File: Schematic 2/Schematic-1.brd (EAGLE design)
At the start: 127.2 x 80.2 mm, 37 parts, among them IC1 7805T, IC3 MCP23017SO, Q1 BSS138, Q2 BSS138, U2 LMV358, U3 LMV324

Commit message: Final tweaks to plugable Tiva board
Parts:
- moved R4 1.38 mm to (55.8, 4.18)
- moved R1 1.32 mm to (55.5, 9.76)
- moved R3 0.20 mm to (55.6, 15.1)
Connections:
- new net N$9: IC3.22, JP4.2
- net N$3: no longer IC3.22
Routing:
- net 37: track 63.5 -> 107.0 mm, vias 5 -> 0
- net 27: track 65.9 -> 100.7 mm, vias 4 -> 2
- net N2: track 97.4 -> 127.4 mm, vias 4 -> 2
- net SCL: track 143.5 -> 113.9 mm, vias 6 -> 8
- net N$9: track 0.00 -> 29.1 mm, vias 0 -> 1
- net 38: track 102.8 -> 75.6 mm, vias 3 -> 2
- net SDA: track 153.8 -> 179.7 mm, vias 6 -> 2
- net 5V1: track 182.7 -> 207.3 mm, vias 6 -> 4
- net 15: track 159.7 -> 135.4 mm
- net 31: track 39.2 -> 62.9 mm
- net 39: track 82.9 -> 65.4 mm, vias 4 -> 3
- net 28: track 39.2 -> 56.4 mm, vias 0 -> 2
- net PB4: track 90.6 -> 74.9 mm
- net PB7: track 92.6 -> 77.2 mm, vias 1 -> 0
- net 30: track 52.1 -> 36.8 mm, vias 4 -> 1
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- added copper zone on layer 1, net GND
- added copper zone on layer 16, net GND
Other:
- board size 127.2 x 80.2 mm -> 127.2 x 82.1 mm
- board text added: "1"
- board text added: "16"
- board text added: "17A"
- board text added: "17B"
- board text added: "3.3V"
- board text added: "55"
- board text added: "57"
- board text added: "5V"
- board text added: "74"
- board text added: "GND"
- board text added: "PORT A"
- board text added: "PORT B"
- board text added: "VBUS"

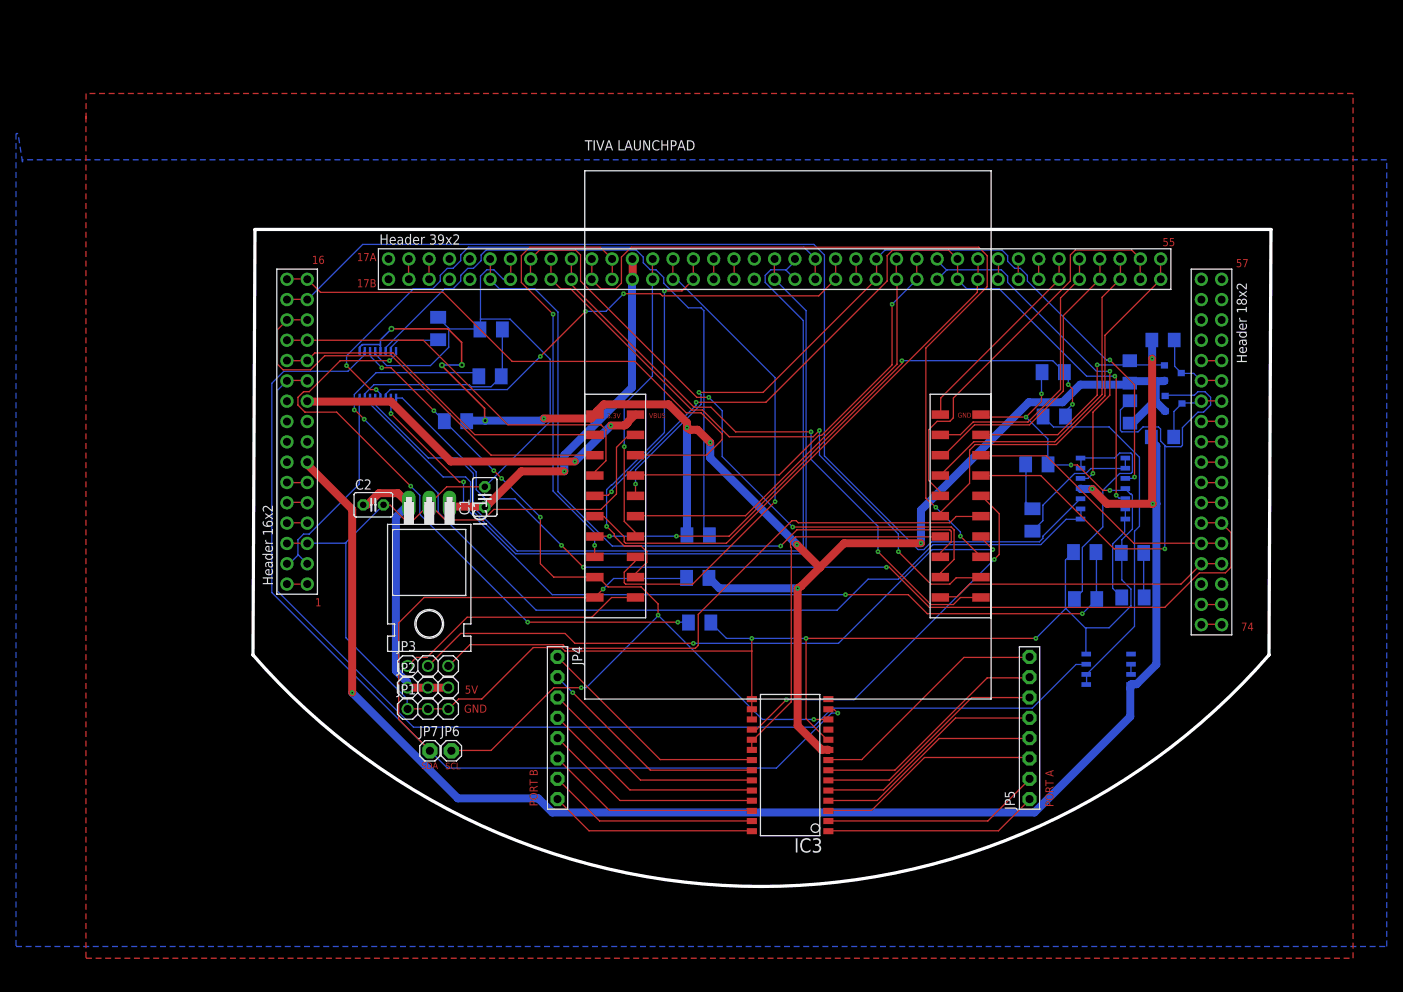
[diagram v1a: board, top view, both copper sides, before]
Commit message: Plugable TIVA board at 17:46
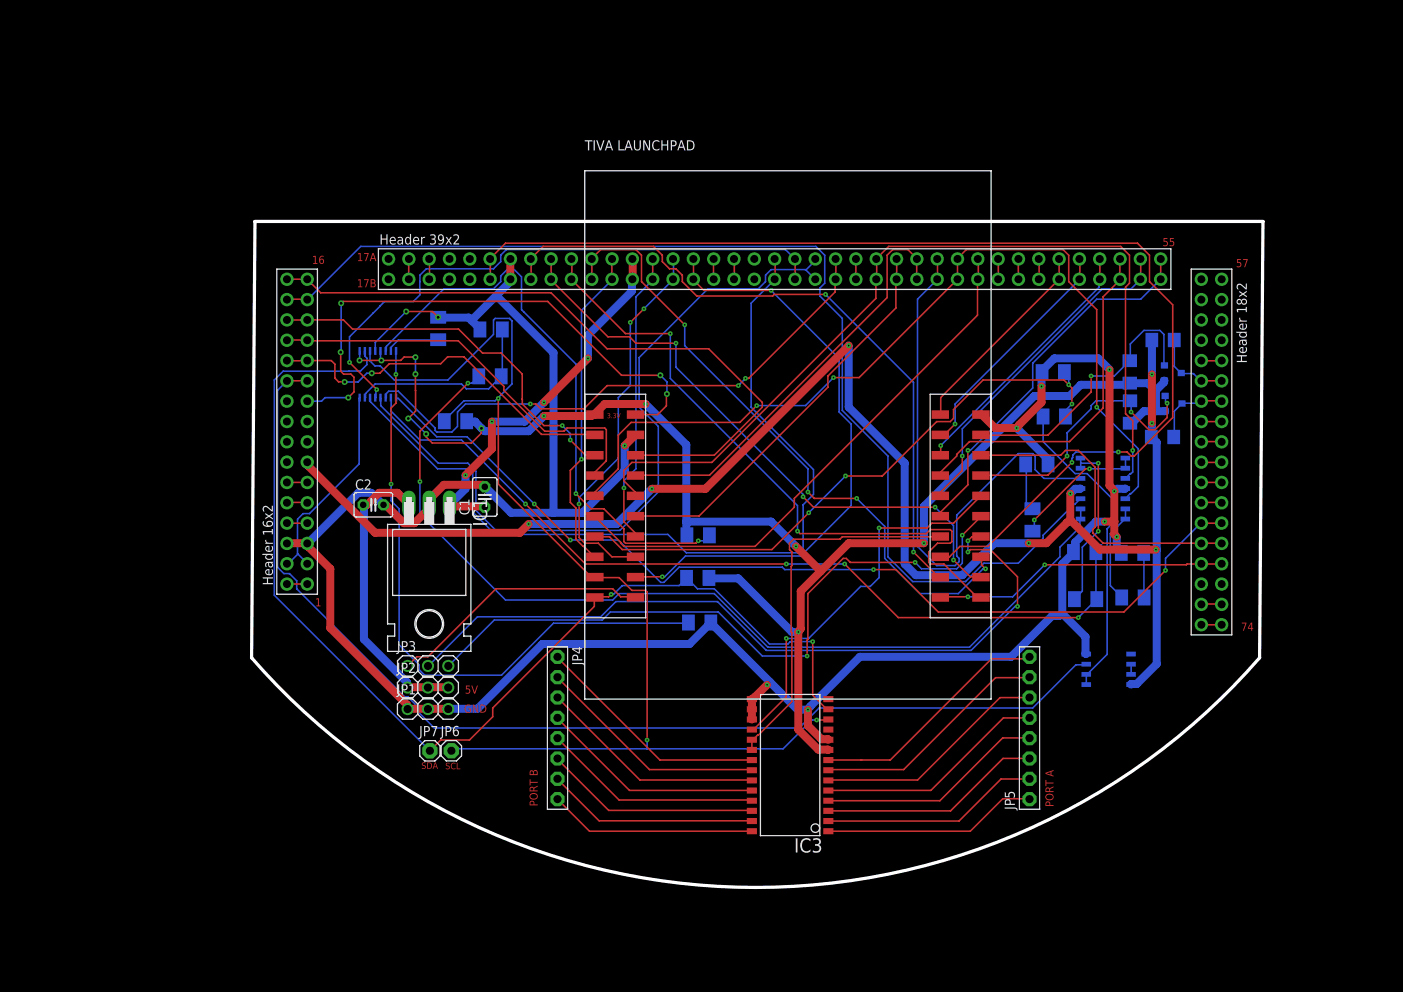
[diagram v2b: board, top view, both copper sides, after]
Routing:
- net 22: track 91.9 -> 145.1 mm, vias 1 -> 2
- net SDA: track 179.7 -> 140.2 mm
- net PF0: track 68.1 -> 34.8 mm, vias 1 -> 3
- net 37: track 107.0 -> 74.3 mm, vias 0 -> 2
- net SCL: track 113.9 -> 146.1 mm, vias 8 -> 3
- net 44: track 45.2 -> 70.3 mm, vias 2 -> 0
- net 32: track 49.5 -> 74.6 mm
- net 5V2: track 46.6 -> 71.1 mm, vias 2 -> 5
- net 27: track 100.7 -> 80.6 mm, vias 2 -> 4
- net 38: track 75.6 -> 94.2 mm, vias 2 -> 0
- net PB6: track 79.9 -> 96.5 mm, vias 2 -> 3
- net 28: track 56.4 -> 40.8 mm, vias 2 -> 1
- net 31: track 62.9 -> 47.8 mm, vias 1 -> 3
- net GND: track 335.9 -> 323.2 mm, vias 7 -> 11
- net 41: track 100.3 -> 110.9 mm, vias 4 -> 1
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- removed copper zone on layer 1, net GND
- removed copper zone on layer 16, net GND
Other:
- board size 127.2 x 82.1 mm -> 126.4 x 83.3 mm
- board text removed: "VBUS"

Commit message: Plugable TIVA changes on 10-6-2017
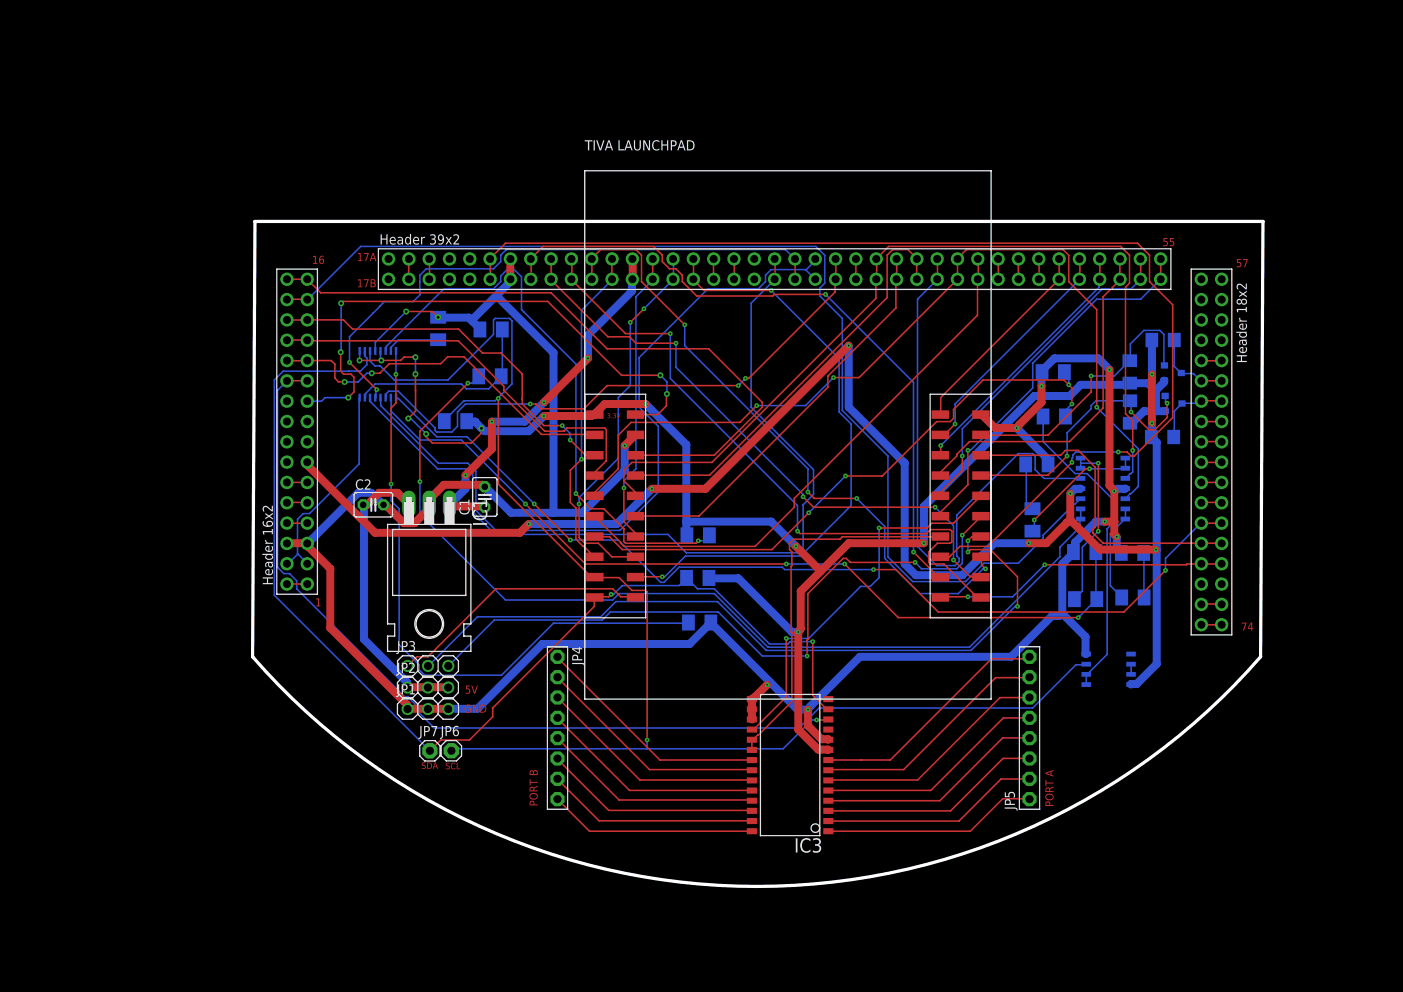
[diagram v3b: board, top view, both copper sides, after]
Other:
- board size 126.4 x 83.3 mm -> 126.3 x 83.1 mm
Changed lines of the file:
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@@
 <board>
 <plain>
-<wire x1="0.182" y1="54.32" x2="-0.2398" y2="-0.2189" width="0.4064" layer="20"/>
-<wire x1="125.7602" y1="-0.2189" x2="126.182" y2="54.32" width="0.4064" layer="20"/>
+<wire x1="0.182" y1="54.32" x2="-0.1134" y2="-0.0924" width="0.4064" layer="20"/>
+<wire x1="125.8866" y1="-0.0924" x2="126.182" y2="54.32" width="0.4064" layer="20"/>
 <wire x1="126.182" y1="54.32" x2="0.182" y2="54.32" width="0.4064" layer="20"/>
-<wire x1="125.7602" y1="-0.2189" x2="-0.2398" y2="-0.2189" width="0.4064" layer="20" curve="-98.003115"/>
+<wire x1="125.8866" y1="-0.0924" x2="-0.1134" y2="-0.0924" width="0.4064" layer="20" curve="-98.003115"/>
 <text x="20.97" y="-14.111" size="0.8128" layer="1">SDA</text>
 <text x="23.966" y="-14.158" size="0.8128" layer="1">SCL</text>

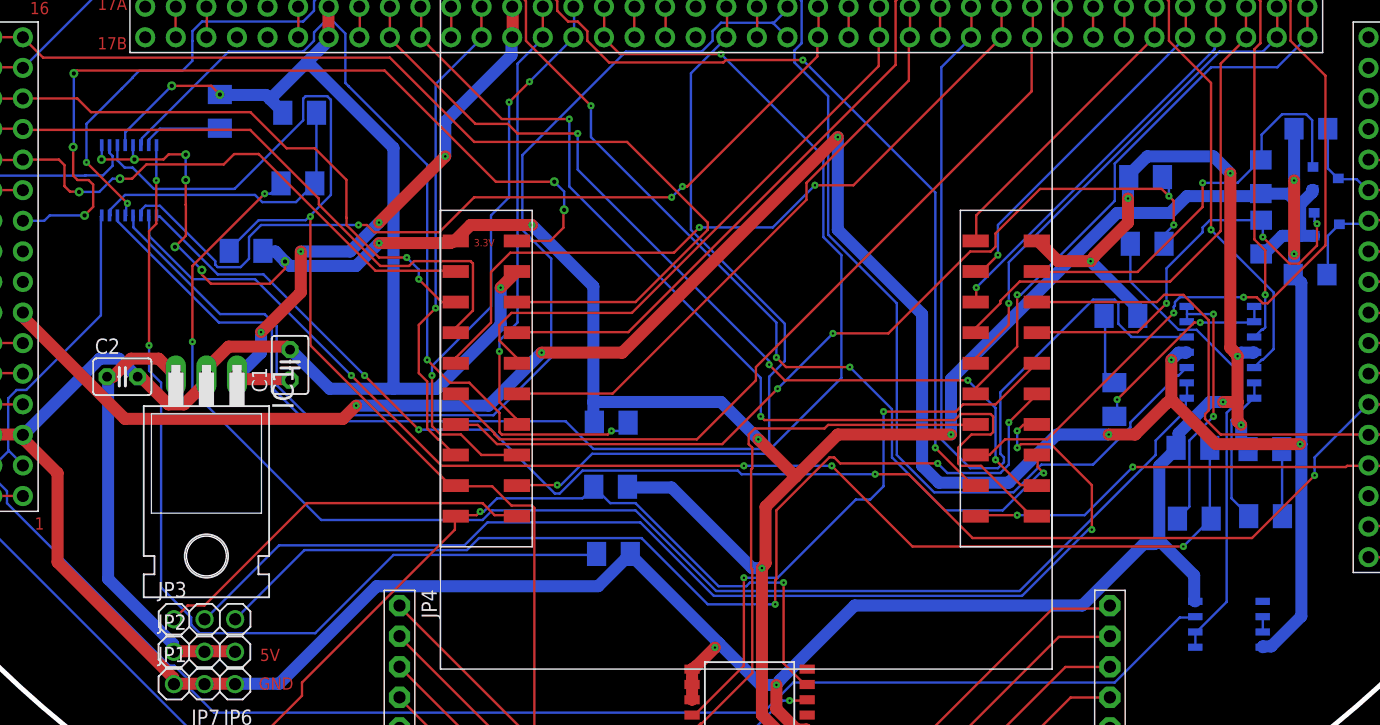
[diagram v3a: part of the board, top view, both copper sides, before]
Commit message: Plugable Tiva board changes at 14:26 on 10-06-2017
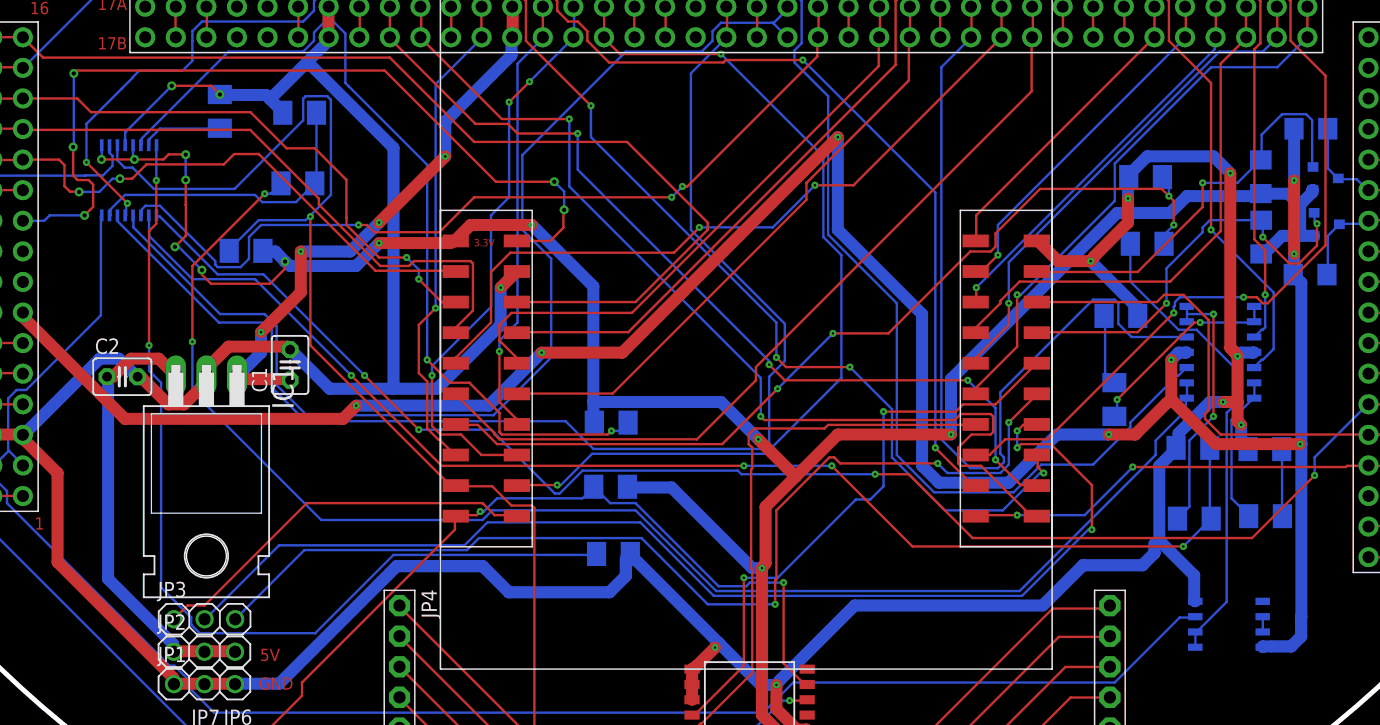
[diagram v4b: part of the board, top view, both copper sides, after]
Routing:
- net GND: track 323.2 -> 326.3 mm
- net 5V1: track 197.8 -> 198.8 mm
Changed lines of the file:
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@@
 <wire x1="107.3" y1="21" x2="107.6" y2="20.6" width="1" layer="1"/>
 <wire x1="75.8" y1="-0.1" x2="69.6" y2="-6.3" width="1" layer="16"/>
-<wire x1="94.7" y1="-0.1" x2="75.8" y2="-0.1" width="1" layer="16"/>
-<wire x1="99.8" y1="5" x2="94.7" y2="-0.1" width="1" layer="16"/>
-<wire x1="100.7" y1="5" x2="99.8" y2="5" width="1" layer="16"/>
+<wire x1="91.4235" y1="-0.1" x2="75.8" y2="-0.1" width="1" layer="16"/>
 <wire x1="69.6" y1="-6.3" x2="69.3" y2="-6.7" width="1" layer="16"/>
 <wire x1="100.7" y1="5" x2="101.1" y2="5.3" width="1" layer="16"/>
@@
 <wire x1="22.1" y1="19.5" x2="21.964" y2="18.996" width="1" layer="1"/>
 <wire x1="28.9" y1="21.2" x2="28.909" y2="21.15" width="1" layer="1"/>
-<wire x1="54.5" y1="1.5" x2="56.8" y2="3.8" width="1" layer="16"/>
-<wire x1="36.1" y1="1.5" x2="54.5" y2="1.5" width="1" layer="16"/>
 <wire x1="28" y1="-6.6" x2="36.1" y2="1.5" width="1" layer="16"/>
 <wire x1="24.4" y1="-6.6" x2="28" y2="-6.6" width="1" layer="16"/>
@@
 <wire x1="22.3593" y1="43.0587" x2="23.08" y2="42.338" width="0.2" layer="1"/>
 <via x="23.08" y="42.338" extent="1-16" drill="0.35"/>
+<wire x1="36.1" y1="1.5" x2="37.7681" y2="3.1681" width="1.016" layer="16"/>
+<wire x1="37.7681" y1="3.1681" x2="44.9081" y2="3.1681" width="1.016" layer="16"/>
+<wire x1="44.9081" y1="3.1681" x2="47.0788" y2="0.9974" width="1.016" layer="16"/>
+<wire x1="47.0788" y1="0.9974" x2="55.4385" y2="0.9974" width="1.016" layer="16"/>
+<wire x1="55.4385" y1="0.9974" x2="56.8" y2="2.3589" width="1.016" layer="16"/>
+<wire x1="56.8" y1="2.3589" x2="56.8" y2="3.8" width="1.016" layer="16"/>
+<wire x1="91.4235" y1="-0.1" x2="94.7634" y2="3.2399" width="1.016" layer="16"/>
+<wire x1="94.7634" y1="3.2399" x2="99.6963" y2="3.2399" width="1.016" layer="16"/>
+<wire x1="99.6963" y1="3.2399" x2="100.7" y2="4.2436" width="1.016" layer="16"/>
+<wire x1="100.7" y1="4.2436" x2="100.7" y2="5" width="1.016" layer="16"/>
 </signal>
 <signal name="PF1">
@@
 <contactref element="R21" pad="1"/>
 <contactref element="R23" pad="1"/>
-<wire x1="110.4" y1="-3.5" x2="109.7" y2="-3.5" width="1" layer="16"/>
-<wire x1="112.9" y1="-1" x2="110.4" y2="-3.5" width="1" layer="16"/>
+<wire x1="109.7" y1="-3.5" x2="110.4" y2="-3.5" width="1" layer="16"/>
 <wire x1="112.9" y1="26.7" x2="112.9" y2="13.3" width="1" layer="16"/>
-<wire x1="112.9" y1="13.3" x2="112.9" y2="-1" width="1" layer="16"/>
+<wire x1="112.9" y1="-1" x2="112.9" y2="13.3" width="1" layer="16"/>
 <wire x1="112.3" y1="27.3" x2="112.9" y2="26.7" width="1" layer="16"/>
 <wire x1="109.7" y1="-3.5" x2="109.691" y2="-3.567" width="1" layer="16"/>
@@
 <via x="74.4" y="38.8" extent="1-16" drill="0.2"/>
 <via x="96.9" y="14.1" extent="1-16" drill="0.2"/>
+<wire x1="110.4" y1="-3.5" x2="112.0594" y2="-3.5" width="1.016" layer="16"/>
+<wire x1="112.0594" y1="-3.5" x2="112.8865" y2="-2.6729" width="1.016" layer="16"/>
+<wire x1="112.8865" y1="-2.6729" x2="112.8865" y2="-1.0135" width="1.016" layer="16"/>
+<wire x1="112.8865" y1="-1.0135" x2="112.9" y2="-1" width="1.016" layer="16"/>
 </signal>
 <signal name="N$2">
@@
 <wire x1="11.1918" y1="44.3276" x2="10.9514" y2="44.0872" width="0.2" layer="1"/>
 <via x="10.9514" y="44.0872" extent="1-16" drill="0.35"/>
-<wire x1="10.9514" y1="44.0872" x2="10.9514" y2="38.0876" width="0.2" layer="16"/>
-<wire x1="10.9514" y1="38.0876" x2="11.0422" y2="37.9968" width="0.2" layer="16"/>
+<wire x1="10.9514" y1="38.0876" x2="10.9514" y2="44.0872" width="0.2" layer="16"/>
 <wire x1="8.4977" y1="31.851" x2="6.719" y2="31.851" width="0.2" layer="16"/>
-<wire x1="11.0422" y1="37.9968" x2="10.9194" y2="37.9968" width="0.2" layer="16"/>
 <wire x1="10.9194" y1="37.9968" x2="10.8969" y2="37.9743" width="0.2" layer="16"/>
 <via x="10.8969" y="37.9743" extent="1-16" drill="0.35"/>
@@
 <wire x1="11.8461" y1="32.2965" x2="8.9432" y2="32.2965" width="0.2" layer="16"/>
 <wire x1="8.9432" y1="32.2965" x2="8.4977" y2="31.851" width="0.2" layer="16"/>
+<wire x1="10.9194" y1="37.9968" x2="10.9514" y2="38.0876" width="0" layer="19" extent="16-16"/>
 </signal>
 <signal name="N$9">
